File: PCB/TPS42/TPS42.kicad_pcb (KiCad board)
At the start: 2 copper layers, 162.9 x 123.9 mm, 83 parts, among them J1 PJ-320A, J10 TP Module, J11 Conn_01x09, J12 Conn_01x09, J13 Conn_01x09, J14 FH12-10S-0.5SH, J2 Conn_01x09, J3 TP Sensor Module, J4 TP Module, J5 TrackPoint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

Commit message: align footprints
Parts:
- removed J10: TP Module, TPS42:TPSensorModule_Connector
- removed J12: Conn_01x09, TPS42:Connector_Reversable_3x3_B
- removed J5: TrackPoint, TPS42:TPModule
- added SW3: Reset, TPS42:SMD-SW-4_5.1x5.1x2.5, F.Cu at (117.2, 100.7)
- J11: value Conn_01x09 -> Conn_01x06; footprint TPS42:Connector_Reversable_3x3_A -> Connector_PinHeader_2.54mm:PinHeader_2x03_P2.54mm_Vertical
- J13, J14, J3: moved to F.Cu
- S12, S5: footprint TPS42:SW_PG1350_reversible -> TPS42:Kailh_socket_PG1350_optional_reversible.kicad_mod
- SW2: footprint TPS42:SW_Tactile_SPST_Angled_PTS645Vx39-2LFS -> TPS42:SMD-SW-4_5.1x5.1x2.5; moved to B.Cu
- moved FB1 115.9 mm to (60.8, 197.4)
- moved C3 99.6 mm to (73.8, 176.9)
- moved R6 92.3 mm to (78.1, 172.4), turned to 0 degrees
- moved J14 90.7 mm to (86.6, 160.4), turned to 0 degrees
- moved C2 90.0 mm to (73.8, 174.4), turned to 0 degrees
- moved C4 88.1 mm to (94.8, 165.5), turned to 0 degrees
- moved FB2 86.3 mm to (90.2, 167.3)
- moved J2 79.0 mm to (84.2, 169.5)
- moved SW2 53.5 mm to (117.2, 100.7), turned to -90 degrees
- moved J6 46.4 mm to (65.0, 194.1)
- moved J13 37.0 mm to (96.3, 160.5), turned to 0 degrees
- moved J1 32.5 mm to (76.9, 157.6), turned to 0 degrees
- moved J3 10.6 mm to (149.0, 91.7)
- moved U8 5.65 mm to (139.3, 50.0)
- moved J11 3.25 mm to (91.2, 93.6), turned to 90 degrees
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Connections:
- net SDA renamed DAT
- J11 pad 2: LCD_DI -> GND
- J11 pad 3: GND -> CLK
- J11 pad 4: SCL -> VCC
- J11 pad 6: VCC -> CS
- J9 pad 1: Net-(J10-Pad1) -> Net-(J3-Pad1)
- J9 pad 2: Net-(J10-Pad2) -> Net-(J3-Pad2)
- J9 pad 3: Net-(J10-Pad3) -> Net-(J3-Pad3)
- J9 pad 4: Net-(J10-Pad4) -> Net-(J3-Pad4)
- R1 pad 2: SCL -> CLK
- U1 pad 1: LCD_DI -> unconnected-(U1-Pad1)
- U1 pad 6: SCL -> CLK
- U1 pad 7: LCD_CS -> CS
- U1 pad 8: LCD_CLK -> unconnected-(U1-Pad8)
- U14 pad 1: LCD_DI -> unconnected-(U14-Pad1)
- U14 pad 6: SCL -> CLK
- U14 pad 7: LCD_CS -> CS
- U14 pad 8: LCD_CLK -> unconnected-(U14-Pad8)
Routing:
- net +3V3: track 57.2 -> 0.00 mm, vias 7 -> 0
- net /DISP: track 35.6 -> 0.00 mm, vias 4 -> 0
- net /SCLK: track 32.9 -> 0.00 mm, vias 3 -> 0
- net Net-(J13-Pad1): track 30.3 -> 0.00 mm, vias 1 -> 0
- net /EXTCOMIN: track 27.7 -> 0.00 mm, vias 1 -> 0
- net /SCS: track 27.1 -> 0.00 mm, vias 1 -> 0
- net /SI: track 24.9 -> 0.00 mm, vias 3 -> 0
- net Net-(J1-Pad2): track 19.9 -> 0.00 mm, vias 1 -> 0
- net GNDA: track 19.2 -> 0.00 mm, vias 1 -> 0
- net VDDA: track 17.0 -> 0.00 mm, vias 1 -> 0
- net Net-(J1-Pad1): track 16.5 -> 0.00 mm
- net /EXTMODE: track 16.4 -> 0.00 mm, vias 3 -> 0
- net Net-(J1-Pad4): track 14.3 -> 0.00 mm, vias 1 -> 0
- net Net-(J13-Pad4): track 13.1 -> 0.00 mm, vias 2 -> 0
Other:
- board size 162.9 x 123.9 mm -> 138.1 x 89.7 mm
- board text added: "S6"
- board text removed: "C5"
- board text removed: "CLK"
- board text removed: "CS"
- board text removed: "DI"
- board text removed: "GND"
- board text removed: "SCL"
- board text removed: "SDA"
- board text removed: "SER"
- board text removed: "VCC"

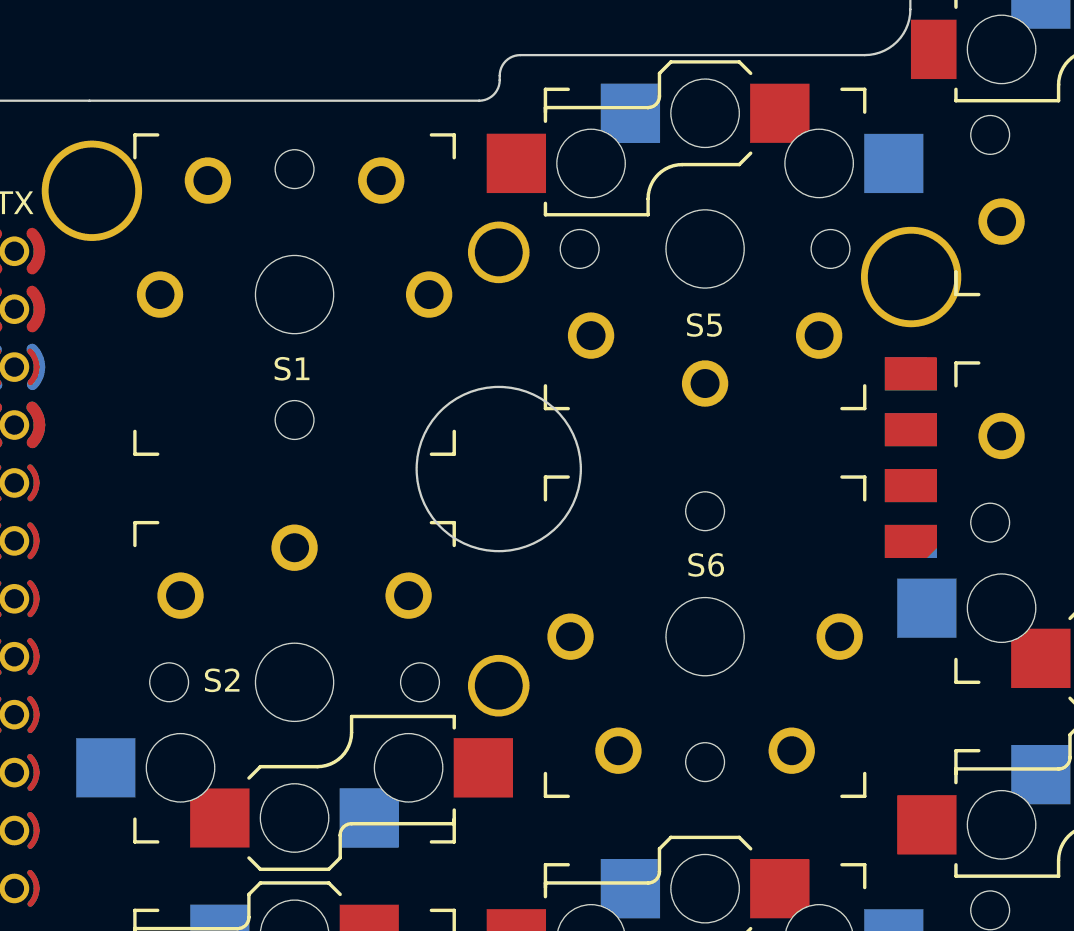
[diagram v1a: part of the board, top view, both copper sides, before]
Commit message: fix switch orientation
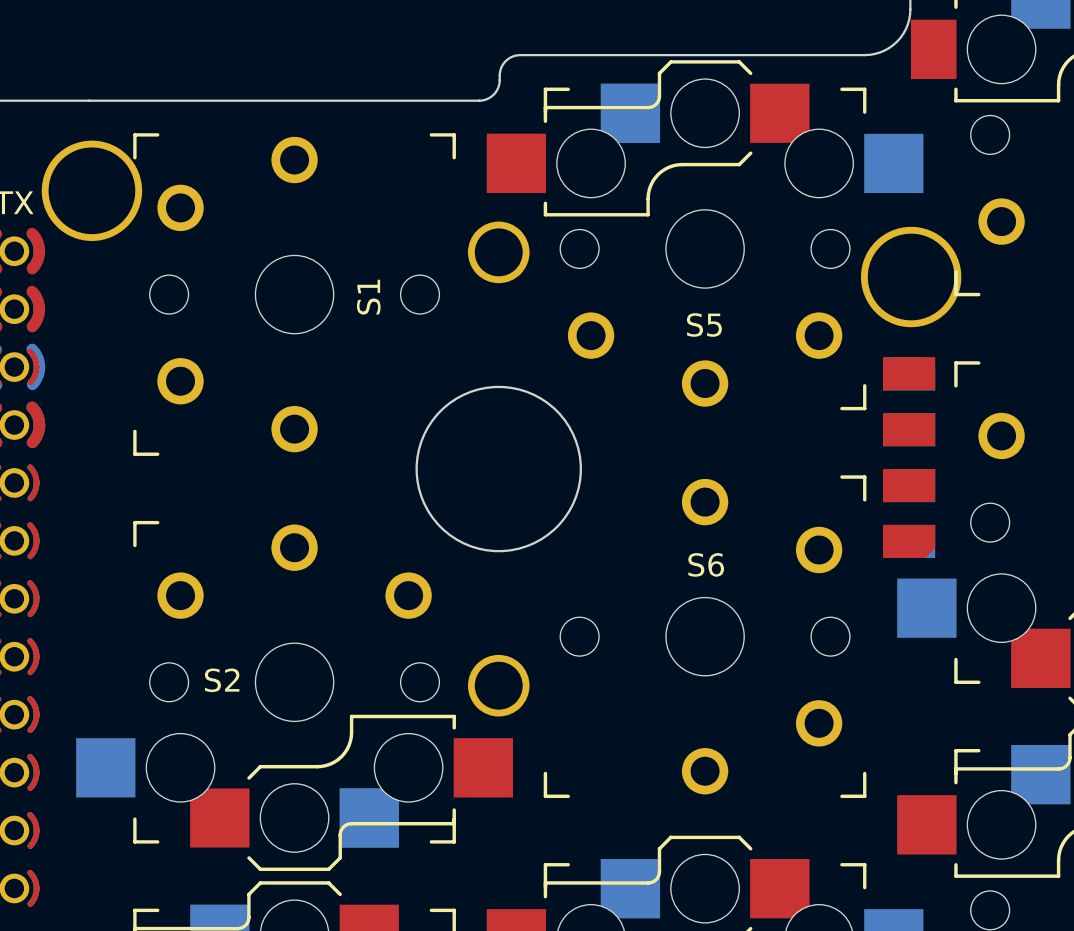
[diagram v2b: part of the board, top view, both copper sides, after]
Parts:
- moved J4 0.08 mm to (139.2, 57.9)
- moved J9 0.08 mm to (139.2, 57.9)
- turned S1 to 180 degrees
- turned S6 to 0 degrees
